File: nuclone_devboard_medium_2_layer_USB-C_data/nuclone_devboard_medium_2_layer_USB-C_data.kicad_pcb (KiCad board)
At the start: 2 copper layers, 50 x 76.2 mm, 41 parts, among them J1 JTAG_2X05, J2 TYPE-C-31-M-12, J3 nuclone_medium_left, J4 nuclone_medium_right, J5 Conn_02x06_Odd_Even, SW1 RESET, SW2 Bootloader, U1 MCP1702-3.3V, U2 TPESD0504C6

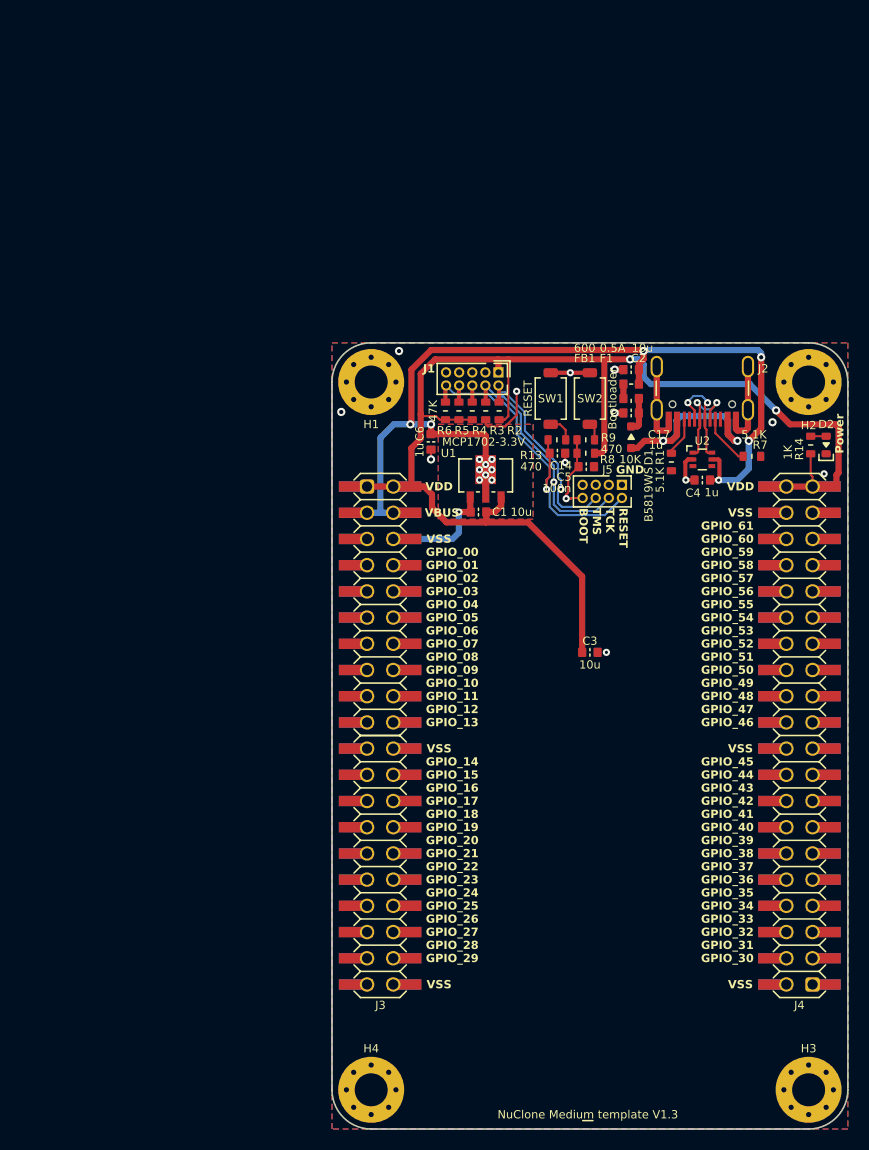
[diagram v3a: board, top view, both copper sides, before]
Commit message: moving board to uniform corner
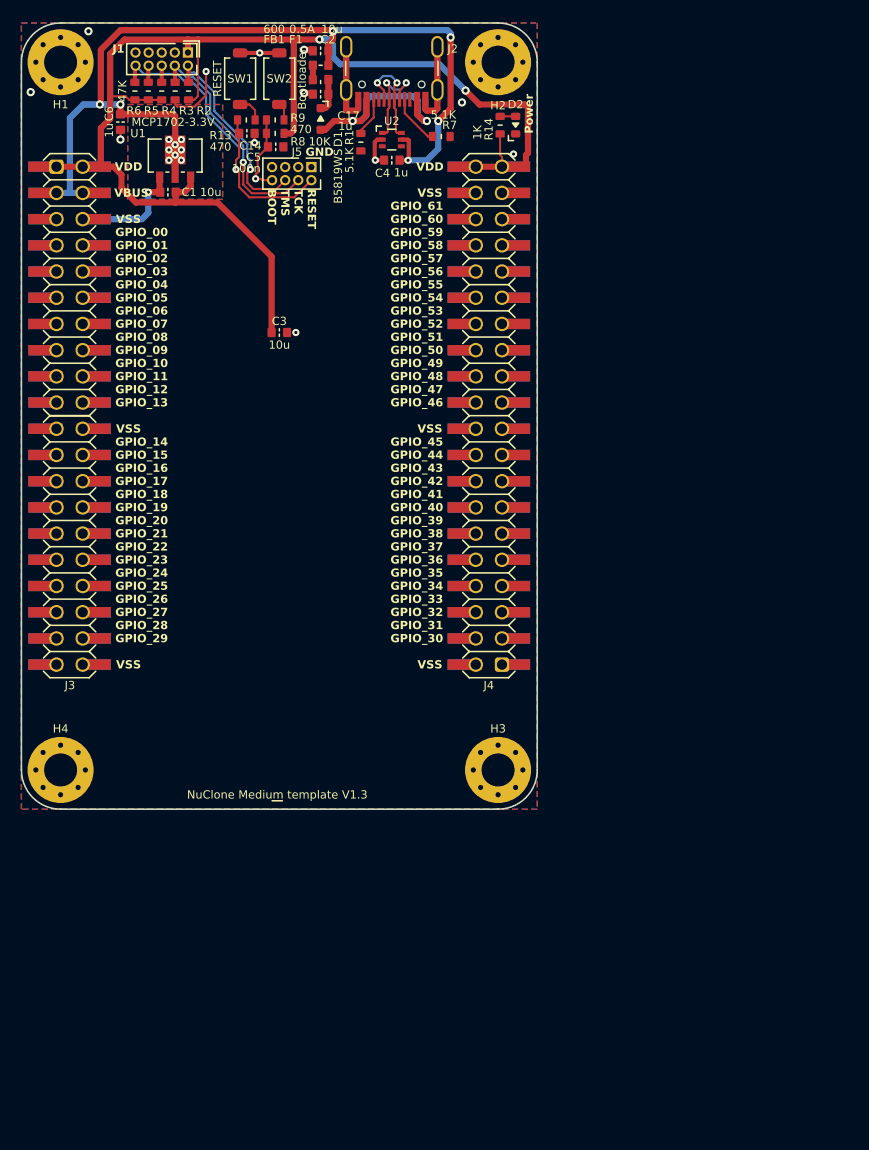
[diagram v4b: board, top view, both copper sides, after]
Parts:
- moved N2 43.2 mm to (54.8, 103.0)
- moved N1 43.2 mm to (54.9, 99.0)
- moved N3 43.2 mm to (54.8, 104.6)
- moved N4 43.2 mm to (54.8, 104.8)
- moved R13 43.2 mm to (51.8, 39.4)
- moved R9 43.2 mm to (54.6, 39.4)
- moved C1 43.2 mm to (44.2, 46.4)
- moved C14 43.2 mm to (51.9, 40.7)
- moved C3 43.2 mm to (55.0, 60.0)
- moved C4 43.2 mm to (65.9, 43.3)
- moved C5 43.2 mm to (54.6, 42.0)
- moved D2 43.2 mm to (77.9, 39.9)
- moved H1 43.2 mm to (33.8, 33.8)
- moved H2 43.2 mm to (76.2, 33.8)
- moved H3 43.2 mm to (76.2, 102.4)
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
